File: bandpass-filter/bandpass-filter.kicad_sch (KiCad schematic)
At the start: 16 parts, among them J1 Amphenol 10118194-0001LF, J2 Conn_Coaxial, J3 Conn_Coaxial, U1 SKY65015-70LF

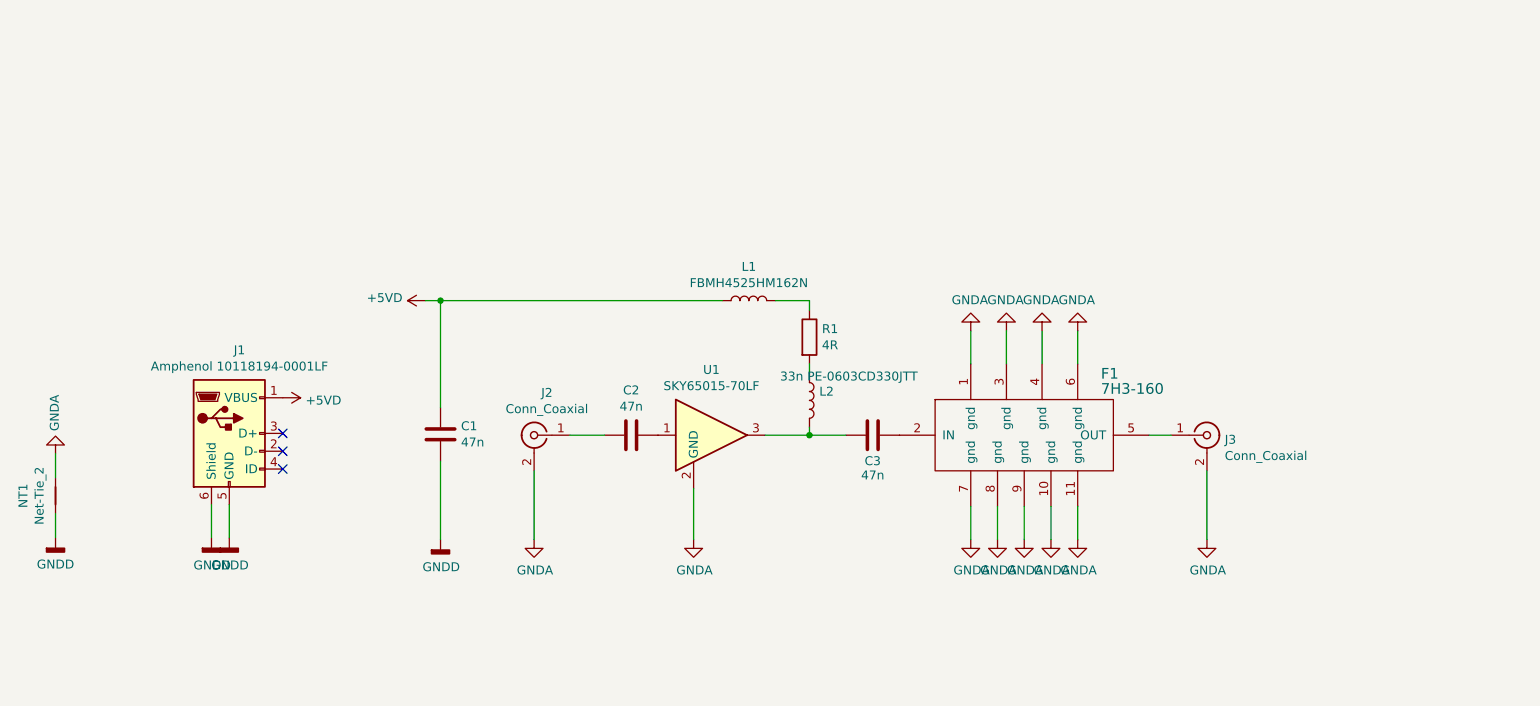
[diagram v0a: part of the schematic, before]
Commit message: Update PCB with controlled impedance JLCPCB process. Change filter and amplifier order
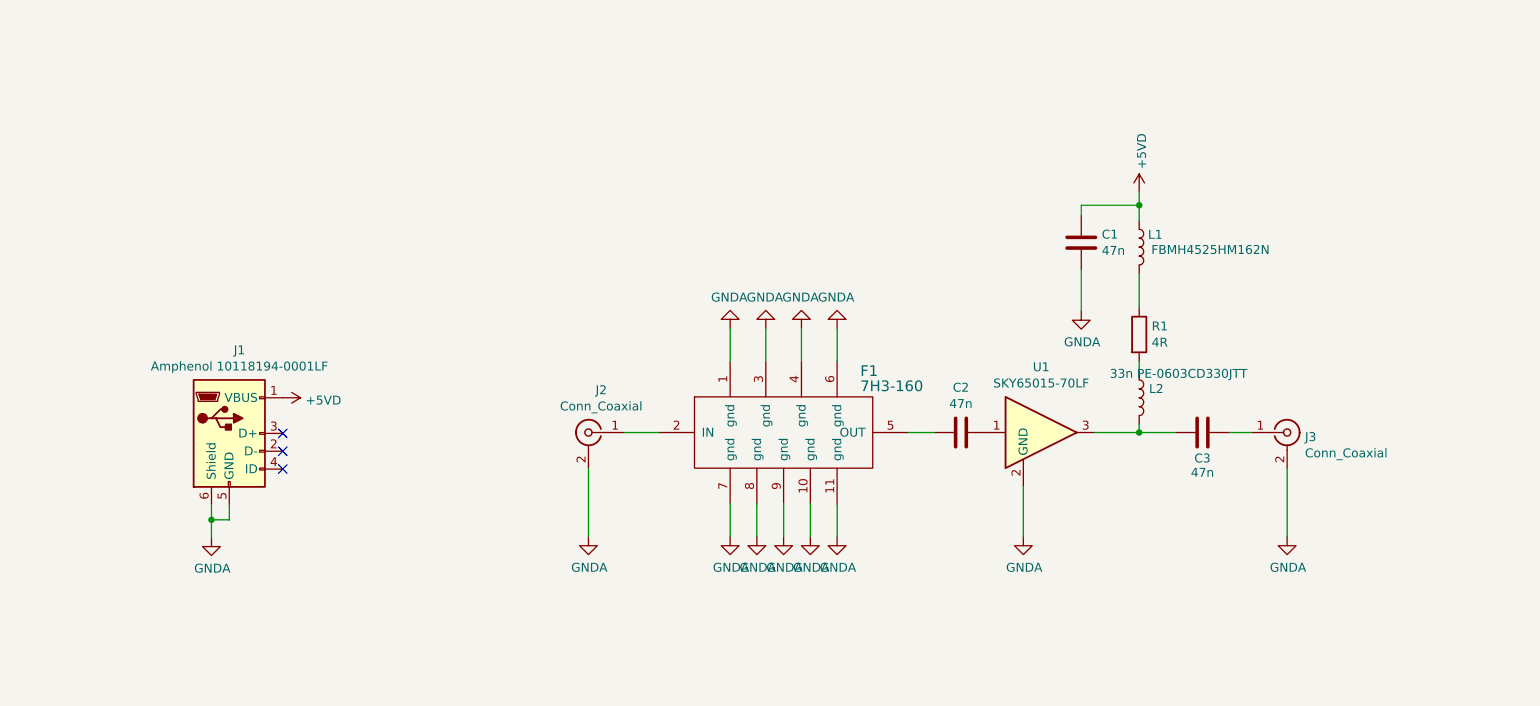
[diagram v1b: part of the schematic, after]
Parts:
- removed NT1: Net-Tie_2, NetTie:NetTie-2_SMD_Pad0.5mm, symbol bandpass-filter-rescue:Net-Tie_2-Device
- J2, J3: footprint Connector_Coaxial:SMA_Molex_73251-2120_EdgeMount_Horizontal -> sma_connector:sma_connector
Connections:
- net GNDD is gone; now on net GNDA: C1.2, J1.5 (GND), J1.6 (Shield)
- net at F1.2 (IN): now also J2.1 (In); no longer C3.1
- net at F1.5 (OUT): now also C2.2; no longer J3.1 (In)
- new net: C3.1, J3.1 (In)
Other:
- moved on the sheet: C1, C2, C3, F1, J2, J3, L1, L2, R1, U1
